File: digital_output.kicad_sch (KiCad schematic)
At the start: 7 parts, among them J12 Conn_Coaxial, U5 74LVC1G17

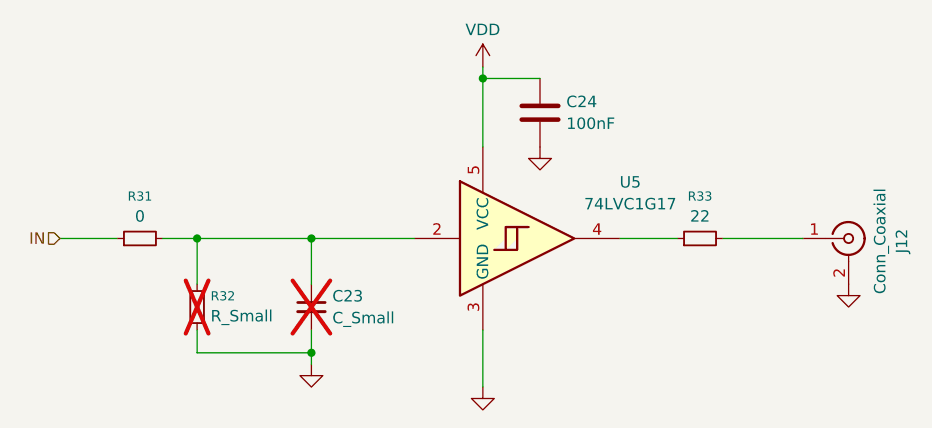
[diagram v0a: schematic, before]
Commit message: adding subproject, breakout board for nucleo
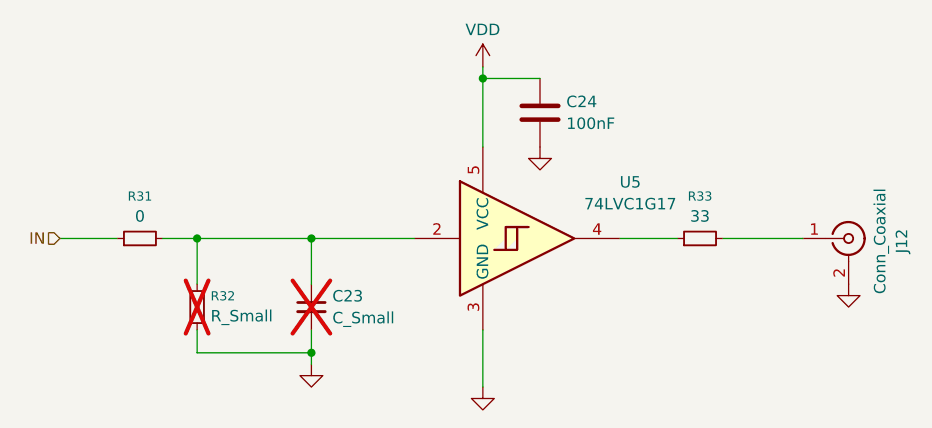
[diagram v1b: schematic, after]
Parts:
- R33: value 22 -> 33
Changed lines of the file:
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@@
 			)
 		)
-		(property "Value" "22"
+		(property "Value" "33"
 			(at 175.26 101.6832 90)
 			(effects
